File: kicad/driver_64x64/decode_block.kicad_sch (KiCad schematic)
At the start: 26 parts

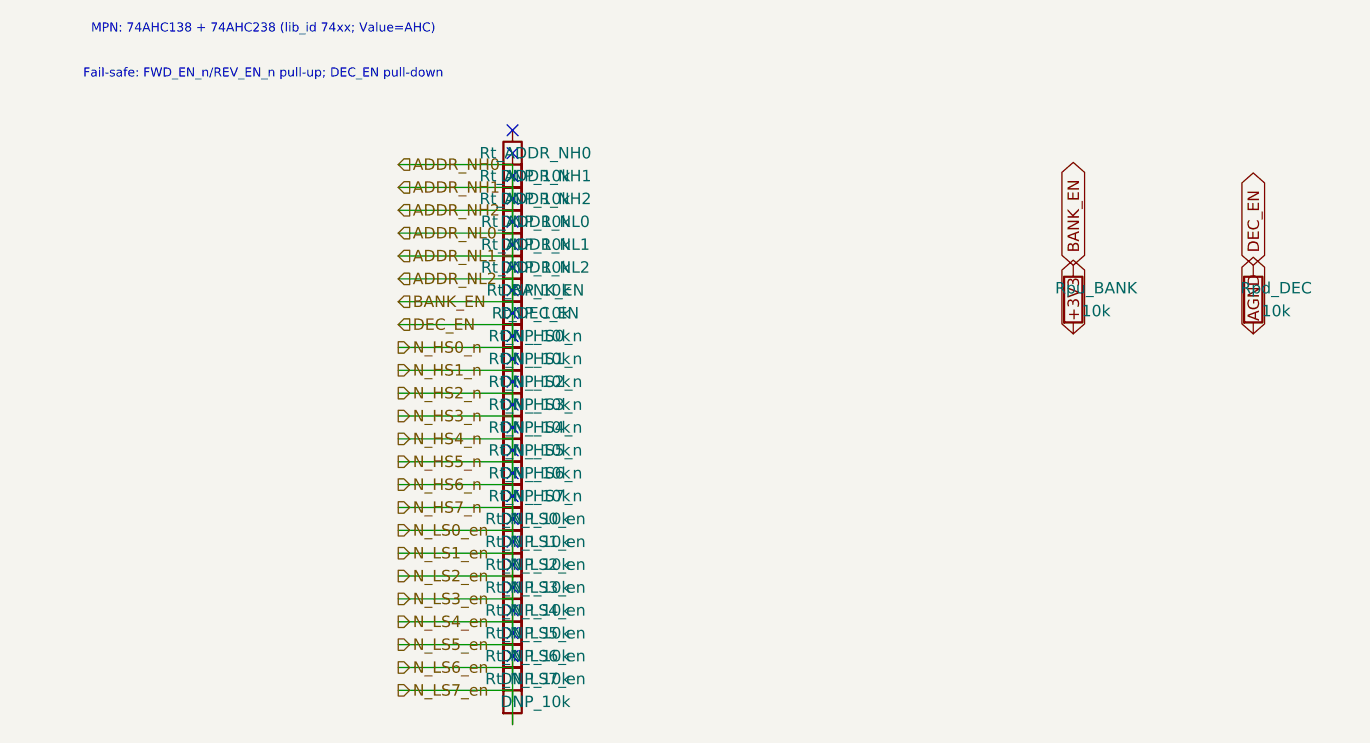
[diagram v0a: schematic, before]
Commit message: logical seperation into host and multiple decode/drive/steering boards
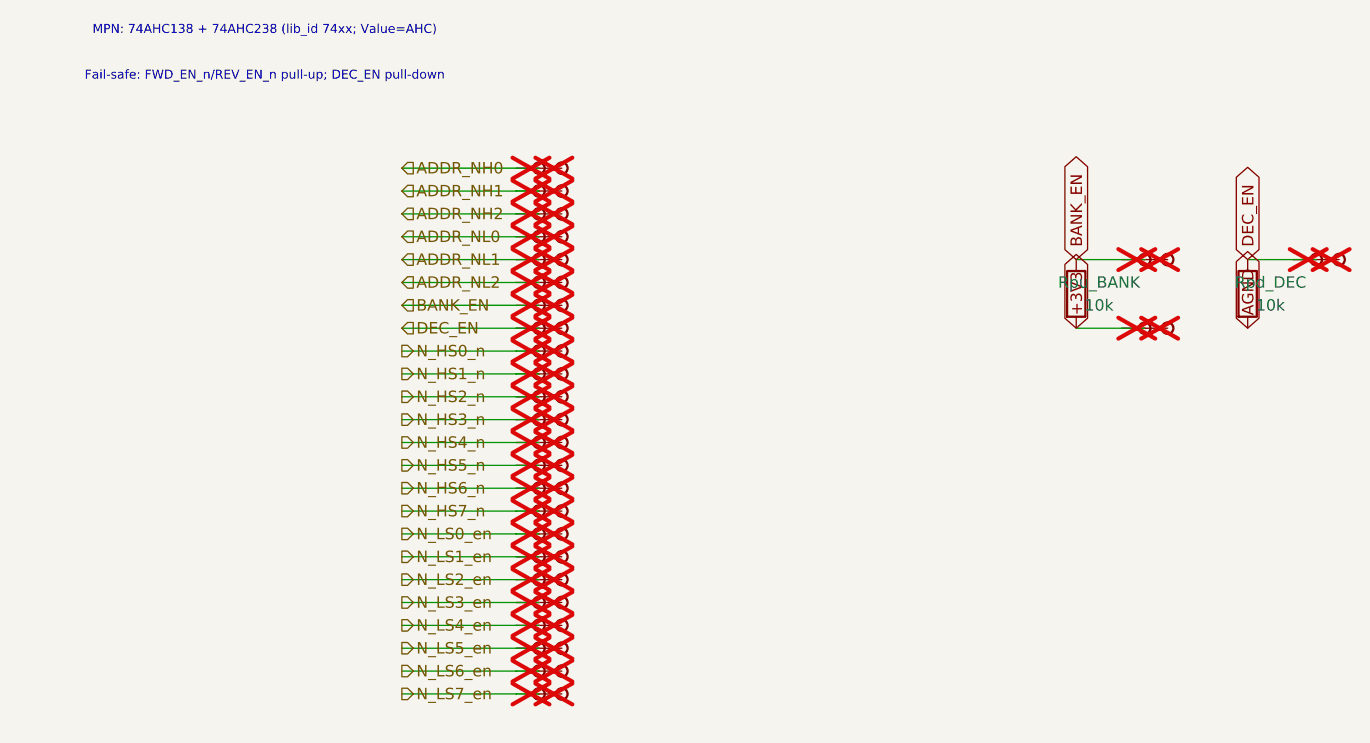
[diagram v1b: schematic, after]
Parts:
- removed Rt_ADDR_NH0, Rt_ADDR_NH1, Rt_ADDR_NH2, Rt_ADDR_NL0, Rt_ADDR_NL1, Rt_ADDR_NL2, Rt_BANK_EN, Rt_DEC_EN, Rt_N_HS0_n, Rt_N_HS1_n, Rt_N_HS2_n, Rt_N_HS3_n, Rt_N_HS4_n, Rt_N_HS5_n, Rt_N_HS6_n, Rt_N_HS7_n, Rt_N_LS0_en, Rt_N_LS1_en, Rt_N_LS2_en, Rt_N_LS3_en, Rt_N_LS4_en, Rt_N_LS5_en, Rt_N_LS6_en, Rt_N_LS7_en: DNP_10k, symbol Device:R
- added TP_ADDR_NH0, TP_ADDR_NH0b, TP_ADDR_NH1, TP_ADDR_NH1b, TP_ADDR_NH2, TP_ADDR_NH2b, TP_ADDR_NL0, TP_ADDR_NL0b, TP_ADDR_NL1, TP_ADDR_NL1b, TP_ADDR_NL2, TP_ADDR_NL2b, TP_BANK_EN, TP_BANK_EN_100_33_35_, TP_BANK_EN_100_33_35_b, TP_BANK_ENb, TP_DEC_EN, TP_DEC_EN_119_38_35_5, TP_DEC_EN_119_38_35_5b, TP_DEC_ENb, TP_N_HS0_n, TP_N_HS0_nb, TP_N_HS1_n, TP_N_HS1_nb, TP_N_HS2_n, TP_N_HS2_nb, TP_N_HS3_n, TP_N_HS3_nb, TP_N_HS4_n, TP_N_HS4_nb, TP_N_HS5_n, TP_N_HS5_nb, TP_N_HS6_n, TP_N_HS6_nb, TP_N_HS7_n, TP_N_HS7_nb, TP_N_LS0_en, TP_N_LS0_enb, TP_N_LS1_en, TP_N_LS1_enb, TP_N_LS2_en, TP_N_LS2_enb, TP_N_LS3_en, TP_N_LS3_enb, TP_N_LS4_en, TP_N_LS4_enb, TP_N_LS5_en, TP_N_LS5_enb, TP_N_LS6_en, TP_N_LS6_enb, TP_N_LS7_en, TP_N_LS7_enb, TP__3V3_100_33_43_18, TP__3V3_100_33_43_18b: Stub, symbol CMR:Stub
- Rpd_DEC, Rpu_BANK: symbol Device:R -> CMR:R
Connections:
- net +3V3: now also TP__3V3_100_33_43_18.1, TP__3V3_100_33_43_18b.1
- net BANK_EN: now also TP_BANK_EN.1, TP_BANK_EN_100_33_35_.1, TP_BANK_EN_100_33_35_b.1, TP_BANK_ENb.1; no longer Rpd_DEC.1
- new net ADDR_NH0: TP_ADDR_NH0.1, TP_ADDR_NH0b.1
- new net ADDR_NH1: TP_ADDR_NH1.1, TP_ADDR_NH1b.1
- new net ADDR_NH2: TP_ADDR_NH2.1, TP_ADDR_NH2b.1
- new net ADDR_NL0: TP_ADDR_NL0.1, TP_ADDR_NL0b.1
- new net ADDR_NL1: TP_ADDR_NL1.1, TP_ADDR_NL1b.1
- new net ADDR_NL2: TP_ADDR_NL2.1, TP_ADDR_NL2b.1
- new net DEC_EN: Rpd_DEC.1, TP_DEC_EN.1, TP_DEC_EN_119_38_35_5.1, TP_DEC_EN_119_38_35_5b.1, TP_DEC_ENb.1
- new net N_HS0_n: TP_N_HS0_n.1, TP_N_HS0_nb.1
- new net N_HS1_n: TP_N_HS1_n.1, TP_N_HS1_nb.1
- new net N_HS2_n: TP_N_HS2_n.1, TP_N_HS2_nb.1
- new net N_HS3_n: TP_N_HS3_n.1, TP_N_HS3_nb.1
- new net N_HS4_n: TP_N_HS4_n.1, TP_N_HS4_nb.1
- new net N_HS5_n: TP_N_HS5_n.1, TP_N_HS5_nb.1
- new net N_HS6_n: TP_N_HS6_n.1, TP_N_HS6_nb.1
- new net N_HS7_n: TP_N_HS7_n.1, TP_N_HS7_nb.1
- new net N_LS0_en: TP_N_LS0_en.1, TP_N_LS0_enb.1
- new net N_LS1_en: TP_N_LS1_en.1, TP_N_LS1_enb.1
- new net N_LS2_en: TP_N_LS2_en.1, TP_N_LS2_enb.1
- new net N_LS3_en: TP_N_LS3_en.1, TP_N_LS3_enb.1
- new net N_LS4_en: TP_N_LS4_en.1, TP_N_LS4_enb.1
- new net N_LS5_en: TP_N_LS5_en.1, TP_N_LS5_enb.1
- new net N_LS6_en: TP_N_LS6_en.1, TP_N_LS6_enb.1
- new net N_LS7_en: TP_N_LS7_en.1, TP_N_LS7_enb.1
- no-connect marks 24 -> 0
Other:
- moved on the sheet: Rpd_DEC, Rpu_BANK
